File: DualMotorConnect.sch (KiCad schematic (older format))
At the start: 2 parts

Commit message: Finish the schematics. All pins are assinged to the NUCLEO-64 board.
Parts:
- renumbered JP1 to JP2, JP2 to JP3
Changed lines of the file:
@@
 	3600 2900 3250 2900
 $Comp
-L Device:Jumper_NO_Small JP1
+L Device:Jumper_NO_Small JP2
 U 1 1 5AD16940
 P 5300 2600
-F 0 "JP1" H 5300 2785 50  0000 C CNN
+F 0 "JP2" H 5300 2785 50  0000 C CNN
 F 1 "Single Z" H 5300 2694 50  0000 C CNN
 F 2 "" H 5300 2600 50  0001 C CNN
@@
 $EndComp
 $Comp
-L Device:Jumper_NO_Small JP2
+L Device:Jumper_NO_Small JP3
 U 1 1 5AD169D3
 P 5350 3800
-F 0 "JP2" H 5350 3985 50  0000 C CNN
+F 0 "JP3" H 5350 3985 50  0000 C CNN
 F 1 "Single Z" H 5350 3894 50  0000 C CNN
 F 2 "" H 5350 3800 50  0001 C CNN

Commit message: Assigned footprints for all components. Inductors are approximate size. MOSFETs dont agree with the footprints. Saved pcb netlist report as report.txt.
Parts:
- JP2, JP3: footprint (none) -> Connector_PinHeader_2.54mm:PinHeader_1x02_P2.54mm_Vertical
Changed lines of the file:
@@
 F 0 "JP2" H 5300 2785 50  0000 C CNN
 F 1 "Single Z" H 5300 2694 50  0000 C CNN
-F 2 "" H 5300 2600 50  0001 C CNN
+F 2 "Connector_PinHeader_2.54mm:PinHeader_1x02_P2.54mm_Vertical" H 5300 2600 50  0001 C CNN
 F 3 "~" H 5300 2600 50  0001 C CNN
 	1    5300 2600
@@
 F 0 "JP3" H 5350 3985 50  0000 C CNN
 F 1 "Single Z" H 5350 3894 50  0000 C CNN
-F 2 "" H 5350 3800 50  0001 C CNN
+F 2 "Connector_PinHeader_2.54mm:PinHeader_1x02_P2.54mm_Vertical" H 5350 3800 50  0001 C CNN
 F 3 "~" H 5350 3800 50  0001 C CNN
 	1    5350 3800

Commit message: Placed motor drivers and some endstops.
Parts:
- removed JP2, JP3: Single Z, Connector_PinHeader_2.54mm:PinHeader_1x02_P2.54mm_Vertical, symbol Device:Jumper_NO_Small
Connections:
- wire segments 18 -> 6
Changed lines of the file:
@@
 F5 "MOT2B" I R 5750 3350 50
 $EndSheet
-Wire Wire Line
-	4450 2900 4750 2900
-Wire Wire Line
-	4450 3350 4750 3350
 Text HLabel 3250 2900 0    50   Input ~ 0
 MOT1A
@@
 MOT2B
 Wire Wire Line
-	5750 2900 5900 2900
-Wire Wire Line
-	5750 3350 5900 3350
-Wire Wire Line
 	3600 3350 3250 3350
 Wire Wire Line
 	3600 2900 3250 2900
-$Comp
-L Device:Jumper_NO_Small JP2
-U 1 1 5AD16940
-P 5300 2600
-F 0 "JP2" H 5300 2785 50  0000 C CNN
-F 1 "Single Z" H 5300 2694 50  0000 C CNN
-F 2 "Connector_PinHeader_2.54mm:PinHeader_1x02_P2.54mm_Vertical" H 5300 2600 50  0001 C CNN
-F 3 "~" H 5300 2600 50  0001 C CNN
-	1    5300 2600
-	1    0    0    -1
-$EndComp
-$Comp
-L Device:Jumper_NO_Small JP3
-U 1 1 5AD169D3
-P 5350 3800
-F 0 "JP3" H 5350 3985 50  0000 C CNN
-F 1 "Single Z" H 5350 3894 50  0000 C CNN
-F 2 "Connector_PinHeader_2.54mm:PinHeader_1x02_P2.54mm_Vertical" H 5350 3800 50  0001 C CNN
-F 3 "~" H 5350 3800 50  0001 C CNN
-	1    5350 3800
-	1    0    0    -1
-$EndComp
 Wire Wire Line
-	4750 3350 4750 3800
+	5750 3350 6050 3350
 Wire Wire Line
-	4750 3800 5250 3800
-Connection ~ 4750 3350
+	4450 3350 4900 3350
 Wire Wire Line
-	4750 3350 4900 3350
+	4450 2900 4900 2900
 Wire Wire Line
-	5450 3800 5900 3800
-Wire Wire Line
-	5900 3800 5900 3350
-Connection ~ 5900 3350
-Wire Wire Line
-	5900 3350 6050 3350
-Wire Wire Line
-	4750 2900 4750 2600
-Wire Wire Line
-	4750 2600 5200 2600
-Connection ~ 4750 2900
-Wire Wire Line
-	4750 2900 4900 2900
-Wire Wire Line
-	5400 2600 5900 2600
-Wire Wire Line
-	5900 2600 5900 2900
-Connection ~ 5900 2900
-Wire Wire Line
-	5900 2900 6050 2900
+	5750 2900 6050 2900
 $EndSCHEMATC

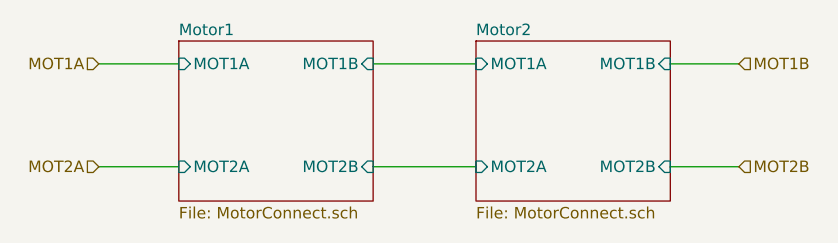
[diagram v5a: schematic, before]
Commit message: Updated motor connector pinout.
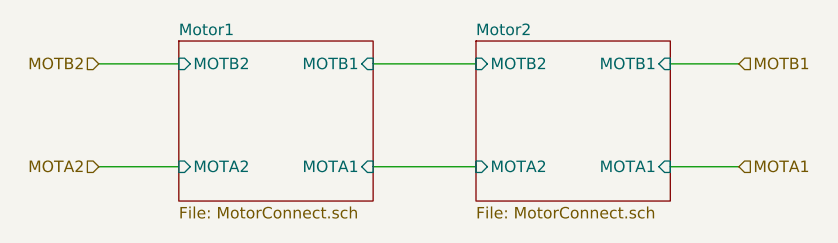
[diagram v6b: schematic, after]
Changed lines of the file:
@@
 F0 "Motor1" 50
 F1 "MotorConnect.sch" 50
-F2 "MOT1B" I R 4450 2900 50
-F3 "MOT1A" I L 3600 2900 50
-F4 "MOT2A" I L 3600 3350 50
-F5 "MOT2B" I R 4450 3350 50
+F2 "MOTB1" I R 4450 2900 50
+F3 "MOTB2" I L 3600 2900 50
+F4 "MOTA2" I L 3600 3350 50
+F5 "MOTA1" I R 4450 3350 50
 $EndSheet
 $Sheet
@@
 F0 "Motor2" 50
 F1 "MotorConnect.sch" 50
-F2 "MOT1B" I R 5750 2900 50
-F3 "MOT1A" I L 4900 2900 50
-F4 "MOT2A" I L 4900 3350 50
-F5 "MOT2B" I R 5750 3350 50
+F2 "MOTB1" I R 5750 2900 50
+F3 "MOTB2" I L 4900 2900 50
+F4 "MOTA2" I L 4900 3350 50
+F5 "MOTA1" I R 5750 3350 50
 $EndSheet
 Text HLabel 3250 2900 0    50   Input ~ 0
-MOT1A
+MOTB2
 Text HLabel 6050 2900 2    50   Input ~ 0
-MOT1B
+MOTB1
 Text HLabel 3250 3350 0    50   Input ~ 0
-MOT2A
+MOTA2
 Text HLabel 6050 3350 2    50   Input ~ 0
-MOT2B
+MOTA1
 Wire Wire Line
 	3600 3350 3250 3350
